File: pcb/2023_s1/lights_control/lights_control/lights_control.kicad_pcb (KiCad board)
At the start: 2 copper layers, 9 parts, among them J1 Conn_01x02_Male, Q1 TIP122, U1 4N25, U2 40106

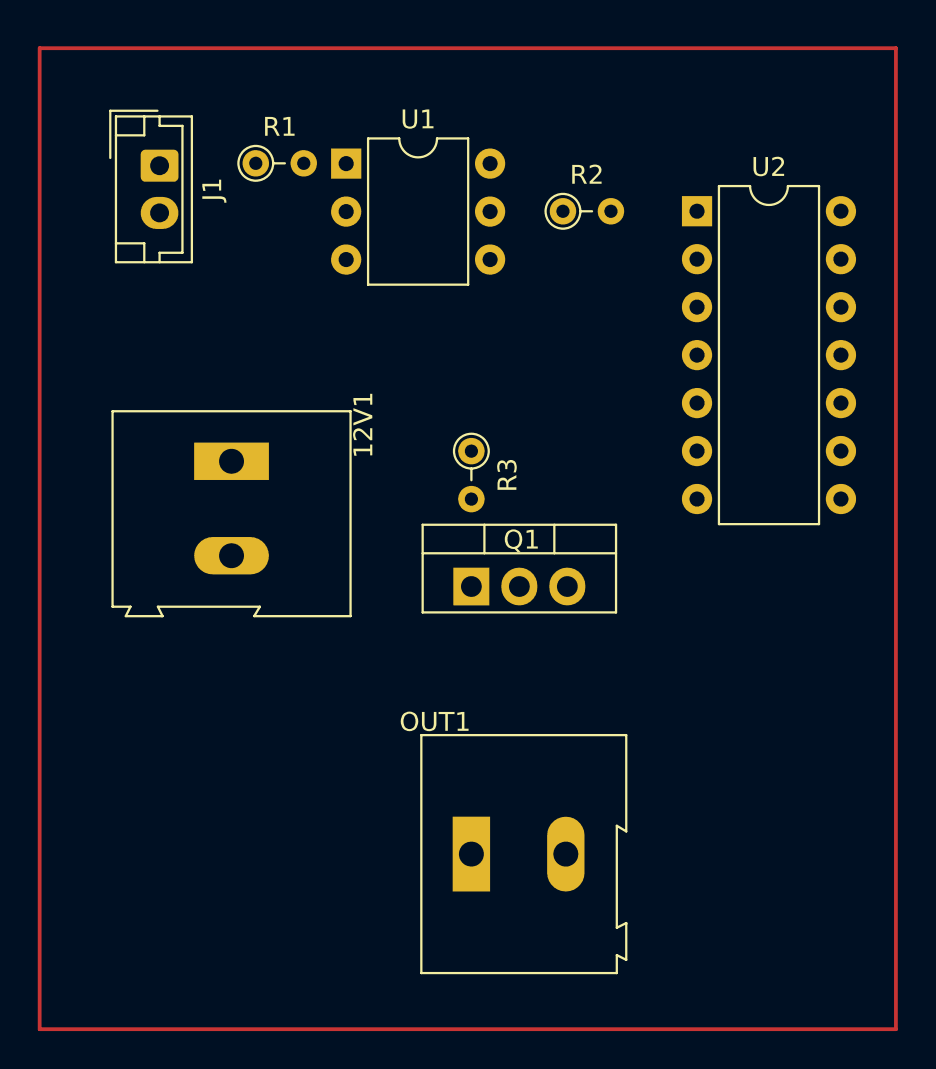
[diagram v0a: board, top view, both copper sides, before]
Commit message: addition, added 3 mounting holes to the pcb, need to add voltage reduction and a better transistor to turn on and off the led lights
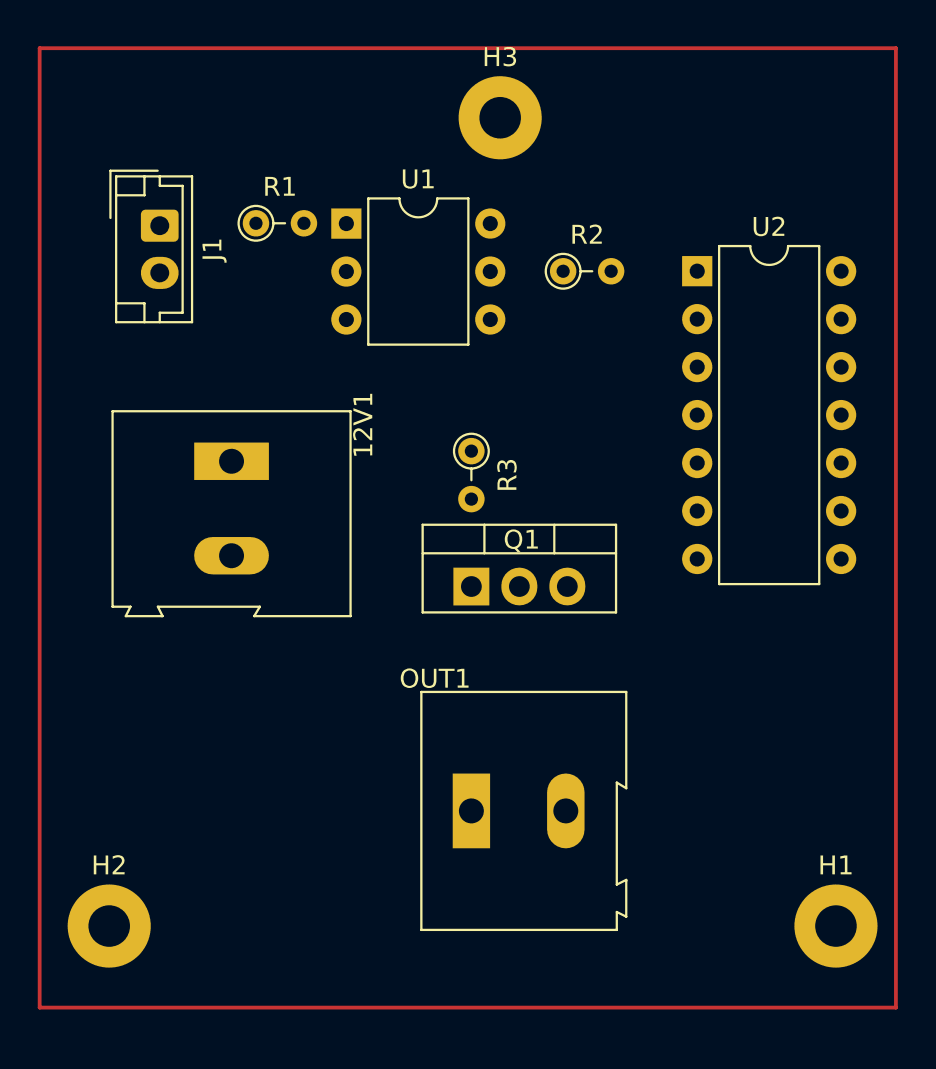
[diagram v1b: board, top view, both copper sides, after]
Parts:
- added H1: MountingHole, MountingHole:MountingHole_2.2mm_M2_Pad, F.Cu at (147.7, 116.1)
- added H2: MountingHole, MountingHole:MountingHole_2.2mm_M2_Pad, F.Cu at (109.2, 116.1)
- added H3: MountingHole, MountingHole:MountingHole_2.2mm_M2_Pad, F.Cu at (129.9, 73.3)
- moved R1 3.18 mm to (117.0, 78.9)
- moved U1 3.18 mm to (121.8, 78.9)
- moved J1 3.18 mm to (111.9, 79.0)
- moved R2 3.18 mm to (133.3, 81.4)
- moved U2 3.18 mm to (140.4, 81.4)
- moved OUT1 2.29 mm to (128.4, 110.0)
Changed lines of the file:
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@@
   (net 19 "unconnected-(U2-Pad10)")
   (net 20 "unconnected-(U2-Pad11)")
+  (footprint "MountingHole:MountingHole_2.2mm_M2_Pad" (layer "F.Cu")
+    (at 129.921 73.279)
+    (descr "Mounting Hole 2.2mm, M2")
+    (tags "mounting hole 2.2mm m2")
+    (property "Sheetfile" "lights_control.kicad_sch")
+    (property "Sheetname" "")
+    (attr exclude_from_pos_files)
+    (fp_text reference "H3" (at 0 -3.2) (layer "F.SilkS")
+      (effects (font (size 1 1) (thickness 0.15)))
+    )
+    (fp_text value "MountingHole" (at 0 3.2) (layer "F.Fab")
+      (effects (font (size 1 1) (thickness 0.15)))
+    )
+    (fp_text user "${REFERENCE}" (at 0 0) (layer "F.Fab")
+      (effects (font (size 1 1) (thickness 0.15)))
+    )
+    (fp_circle (center 0 0) (end 2.2 0) (layer "Cmts.User") (width 0.15) (fill none))
+    (fp_circle (center 0 0) (end 2.45 0) (layer "F.CrtYd") (width 0.05) (fill none))
+    (pad "1" thru_hole circle (at 0 0) (size 4.4 4.4) (drill 2.2) (layers *.Cu *.Mask))
+  )
   (footprint "TerminalBlock:TerminalBlock_Altech_AK300-2_P5.00mm" (layer "F.Cu")
     (at 115.697 91.469 -90)
@@
   )
   (footprint "Connector_JST:JST_EH_B2B-EH-A_1x02_P2.50mm_Vertical" (layer "F.Cu")
-    (at 111.887 75.819 -90)
+    (at 111.897 78.994 -90)
     (descr "JST EH series connector, B2B-EH-A (http://www.jst-mfg.com/product/pdf/eng/eEH.pdf), generated with kicad-footprint-generator")
     (tags "connector JST EH vertical")
@@
   )
   (footprint "Resistor_THT:R_Axial_DIN0204_L3.6mm_D1.6mm_P2.54mm_Vertical" (layer "F.Cu")
-    (at 116.981 75.692)
+    (at 116.991 78.867)
     (descr "Resistor, Axial_DIN0204 series, Axial, Vertical, pin pitch=2.54mm, 0.167W, length*diameter=3.6*1.6mm^2, http://cdn-reichelt.de/documents/datenblatt/B400/1_4W%23YAG.pdf")
     (tags "Resistor Axial_DIN0204 series Axial Vertical pin pitch 2.54mm 0.167W length 3.6mm diameter 1.6mm")
@@
   )
   (footprint "Package_DIP:DIP-14_W7.62mm" (layer "F.Cu")
-    (at 140.345 78.227)
+    (at 140.355 81.402)
     (descr "14-lead though-hole mounted DIP package, row spacing 7.62 mm (300 mils)")
     (tags "THT DIP DIL PDIP 2.54mm 7.62mm 300mil")
@@
     )
   )
+  (footprint "MountingHole:MountingHole_2.2mm_M2_Pad" (layer "F.Cu")
+    (at 147.701 116.078)
+    (descr "Mounting Hole 2.2mm, M2")
+    (tags "mounting hole 2.2mm m2")
+    (property "Sheetfile" "lights_control.kicad_sch")
+    (property "Sheetname" "")
+    (attr exclude_from_pos_files)
+    (fp_text reference "H1" (at 0 -3.2) (layer "F.SilkS")
+      (effects (font (size 1 1) (thickness 0.15)))
+    )
+    (fp_text value "MountingHole" (at 0 3.2) (layer "F.Fab")
+      (effects (font (size 1 1) (thickness 0.15)))
+    )
+    (fp_text user "${REFERENCE}" (at 0 0) (layer "F.Fab")
+      (effects (font (size 1 1) (thickness 0.15)))
+    )
+    (fp_circle (center 0 0) (end 2.2 0) (layer "Cmts.User") (width 0.15) (fill none))
+    (fp_circle (center 0 0) (end 2.45 0) (layer "F.CrtYd") (width 0.05) (fill none))
+    (pad "1" thru_hole circle (at 0 0) (size 4.4 4.4) (drill 2.2) (layers *.Cu *.Mask))
+  )
+  (footprint "MountingHole:MountingHole_2.2mm_M2_Pad" (layer "F.Cu")
+    (at 109.22 116.078)
+    (descr "Mounting Hole 2.2mm, M2")
+    (tags "mounting hole 2.2mm m2")
+    (property "Sheetfile" "lights_control.kicad_sch")
+    (property "Sheetname" "")
+    (attr exclude_from_pos_files)
+    (fp_text reference "H2" (at 0 -3.2) (layer "F.SilkS")
+      (effects (font (size 1 1) (thickness 0.15)))
+    )
+    (fp_text value "MountingHole" (at 0 3.2) (layer "F.Fab")
+      (effects (font (size 1 1) (thickness 0.15)))
+    )
+    (fp_text user "${REFERENCE}" (at 0 0) (layer "F.Fab")
+      (effects (font (size 1 1) (thickness 0.15)))
+    )
+    (fp_circle (center 0 0) (end 2.2 0) (layer "Cmts.User") (width 0.15) (fill none))
+    (fp_circle (center 0 0) (end 2.45 0) (layer "F.CrtYd") (width 0.05) (fill none))
+    (pad "1" thru_hole circle (at 0 0) (size 4.4 4.4) (drill 2.2) (layers *.Cu *.Mask))
+  )
   (footprint "Resistor_THT:R_Axial_DIN0204_L3.6mm_D1.6mm_P2.54mm_Vertical" (layer "F.Cu")
     (at 128.397 90.932 -90)
@@
   )
   (footprint "Package_DIP:DIP-6_W7.62mm" (layer "F.Cu")
-    (at 121.767 75.707)
+    (at 121.777 78.882)
     (descr "6-lead though-hole mounted DIP package, row spacing 7.62 mm (300 mils)")
     (tags "THT DIP DIL PDIP 2.54mm 7.62mm 300mil")
@@
   )
   (footprint "TerminalBlock:TerminalBlock_Altech_AK300-2_P5.00mm" (layer "F.Cu")
-    (at 128.397 112.268)
+    (at 128.397 109.982)
     (descr "Altech AK300 terminal block, pitch 5.0mm, 45 degree angled, see http://www.mouser.com/ds/2/16/PCBMETRC-24178.pdf")
     (tags "Altech AK300 terminal block pitch 5.0mm")
@@
   )
   (footprint "Resistor_THT:R_Axial_DIN0204_L3.6mm_D1.6mm_P2.54mm_Vertical" (layer "F.Cu")
-    (at 133.246 78.232)
+    (at 133.256 81.407)
     (descr "Resistor, Axial_DIN0204 series, Axial, Vertical, pin pitch=2.54mm, 0.167W, length*diameter=3.6*1.6mm^2, http://cdn-reichelt.de/documents/datenblatt/B400/1_4W%23YAG.pdf")
     (tags "Resistor Axial_DIN0204 series Axial Vertical pin pitch 2.54mm 0.167W length 3.6mm diameter 1.6mm")
@@
     )
   )
-  (gr_rect (start 150.876 69.596) (end 105.537 121.539) (layer "F.Cu") (width 0.2) (fill none))
+  (gr_rect (start 150.876 69.596) (end 105.537 120.396) (layer "F.Cu") (width 0.2) (fill none))
 )

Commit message: update, new export files and added voltage elevator space for lights control pcb
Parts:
- added H4: MountingHole, MountingHole:MountingHole_2.2mm_M2_Pad, F.Cu at (91.3, 116.2)
- added H5: MountingHole, MountingHole:MountingHole_2.2mm_M2_Pad, F.Cu at (64.0, 116.2)
- added H6: MountingHole, MountingHole:MountingHole_2.2mm_M2_Pad, F.Cu at (91.5, 59.1)
- added H7: MountingHole, MountingHole:MountingHole_2.2mm_M2_Pad, F.Cu at (64.2, 59.1)
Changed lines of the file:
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@@
     )
+  )
+  (footprint "MountingHole:MountingHole_2.2mm_M2_Pad" (layer "F.Cu")
+    (at 64.22 59.1)
+    (descr "Mounting Hole 2.2mm, M2")
+    (tags "mounting hole 2.2mm m2")
+    (property "Sheetfile" "lights_control.kicad_sch")
+    (property "Sheetname" "")
+    (attr exclude_from_pos_files)
+    (fp_text reference "H7" (at 0 -3.2) (layer "F.SilkS")
+      (effects (font (size 1 1) (thickness 0.15)))
+    )
+    (fp_text value "MountingHole" (at 0 3.2) (layer "F.Fab")
+      (effects (font (size 1 1) (thickness 0.15)))
+    )
+    (fp_text user "${REFERENCE}" (at 0 0) (layer "F.Fab")
+      (effects (font (size 1 1) (thickness 0.15)))
+    )
+    (fp_circle (center 0 0) (end 2.2 0) (layer "Cmts.User") (width 0.15) (fill none))
+    (fp_circle (center 0 0) (end 2.45 0) (layer "F.CrtYd") (width 0.05) (fill none))
+    (pad "1" thru_hole circle (at 0 0) (size 4.4 4.4) (drill 2.2) (layers *.Cu *.Mask))
   )
   (footprint "Package_TO_SOT_THT:TO-220-3_Vertical" (layer "F.Cu")
@@
       (rotate (xyz 0 0 0))
     )
+  )
+  (footprint "MountingHole:MountingHole_2.2mm_M2_Pad" (layer "F.Cu")
+    (at 64.02 116.2)
+    (descr "Mounting Hole 2.2mm, M2")
+    (tags "mounting hole 2.2mm m2")
+    (property "Sheetfile" "lights_control.kicad_sch")
+    (property "Sheetname" "")
+    (attr exclude_from_pos_files)
+    (fp_text reference "H5" (at 0 -3.2) (layer "F.SilkS")
+      (effects (font (size 1 1) (thickness 0.15)))
+    )
+    (fp_text value "MountingHole" (at 0 3.2) (layer "F.Fab")
+      (effects (font (size 1 1) (thickness 0.15)))
+    )
+    (fp_text user "${REFERENCE}" (at 0 0) (layer "F.Fab")
+      (effects (font (size 1 1) (thickness 0.15)))
+    )
+    (fp_circle (center 0 0) (end 2.2 0) (layer "Cmts.User") (width 0.15) (fill none))
+    (fp_circle (center 0 0) (end 2.45 0) (layer "F.CrtYd") (width 0.05) (fill none))
+    (pad "1" thru_hole circle (at 0 0) (size 4.4 4.4) (drill 2.2) (layers *.Cu *.Mask))
   )
   (footprint "Resistor_THT:R_Axial_DIN0204_L3.6mm_D1.6mm_P2.54mm_Vertical" (layer "F.Cu")
@@
       (rotate (xyz 0 0 0))
     )
+  )
+  (footprint "MountingHole:MountingHole_2.2mm_M2_Pad" (layer "F.Cu")
+    (at 91.3 116.2)
+    (descr "Mounting Hole 2.2mm, M2")
+    (tags "mounting hole 2.2mm m2")
+    (property "Sheetfile" "lights_control.kicad_sch")
+    (property "Sheetname" "")
+    (attr exclude_from_pos_files)
+    (fp_text reference "H4" (at 0 -3.2) (layer "F.SilkS")
+      (effects (font (size 1 1) (thickness 0.15)))
+    )
+    (fp_text value "MountingHole" (at 0 3.2) (layer "F.Fab")
+      (effects (font (size 1 1) (thickness 0.15)))
+    )
+    (fp_text user "${REFERENCE}" (at 0 0) (layer "F.Fab")
+      (effects (font (size 1 1) (thickness 0.15)))
+    )
+    (fp_circle (center 0 0) (end 2.2 0) (layer "Cmts.User") (width 0.15) (fill none))
+    (fp_circle (center 0 0) (end 2.45 0) (layer "F.CrtYd") (width 0.05) (fill none))
+    (pad "1" thru_hole circle (at 0 0) (size 4.4 4.4) (drill 2.2) (layers *.Cu *.Mask))
   )
   (footprint "Package_DIP:DIP-6_W7.62mm" (layer "F.Cu")
@@
     )
   )
-  (gr_rect (start 150.876 69.596) (end 105.537 120.396) (layer "F.Cu") (width 0.2) (fill none))
+  (footprint "MountingHole:MountingHole_2.2mm_M2_Pad" (layer "F.Cu")
+    (at 91.5 59.1)
+    (descr "Mounting Hole 2.2mm, M2")
+    (tags "mounting hole 2.2mm m2")
+    (property "Sheetfile" "lights_control.kicad_sch")
+    (property "Sheetname" "")
+    (attr exclude_from_pos_files)
+    (fp_text reference "H6" (at 0 -3.2) (layer "F.SilkS")
+      (effects (font (size 1 1) (thickness 0.15)))
+    )
+    (fp_text value "MountingHole" (at 0 3.2) (layer "F.Fab")
+      (effects (font (size 1 1) (thickness 0.15)))
+    )
+    (fp_text user "${REFERENCE}" (at 0 0) (layer "F.Fab")
+      (effects (font (size 1 1) (thickness 0.15)))
+    )
+    (fp_circle (center 0 0) (end 2.2 0) (layer "Cmts.User") (width 0.15) (fill none))
+    (fp_circle (center 0 0) (end 2.45 0) (layer "F.CrtYd") (width 0.05) (fill none))
+    (pad "1" thru_hole circle (at 0 0) (size 4.4 4.4) (drill 2.2) (layers *.Cu *.Mask))
+  )
+  (gr_rect (start 150.876 52.346) (end 56.287 121.396) (layer "F.Cu") (width 0.2) (fill none))
+  (gr_rect (start 59.4 54.85) (end 96.25 120) (layer "F.SilkS") (width 0.2) (fill none))
+  (group "" (id 00337593-777a-4c58-88cc-cdb5a021b062)
+    (members
+      187c98bf-b8d1-4bf8-a18b-adc7ccf804a8
+      e91737d2-66c0-4c66-9fda-42e3aaefe411
+    )
+  )
+  (group "" (id 7de41c36-1b53-434b-914d-120d0a8890b0)
+    (members
+      6e19ae29-2da6-47ad-aa21-1ab7fbc4f013
+      985ad4b4-784b-4b28-a9a1-c418e2ce8c57
+    )
+  )
 )

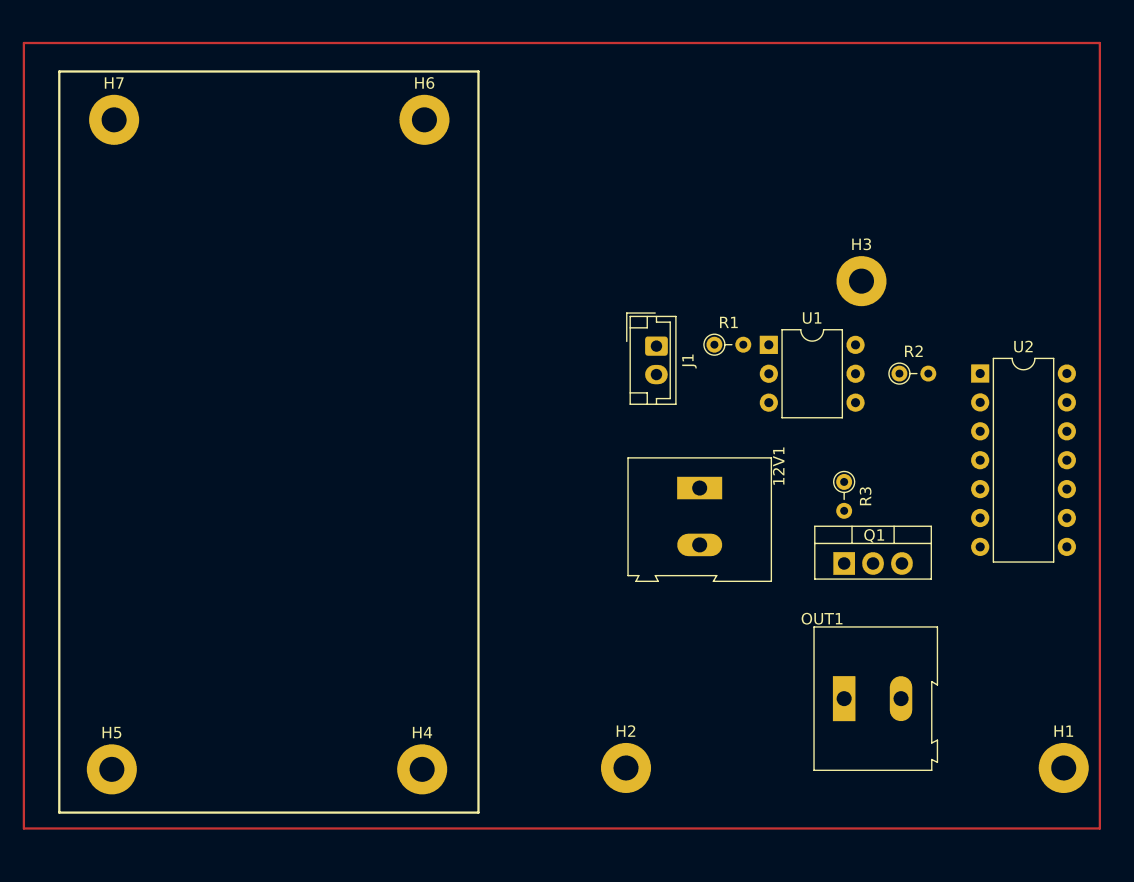
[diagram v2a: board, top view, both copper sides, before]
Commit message: update, routed lights pcb
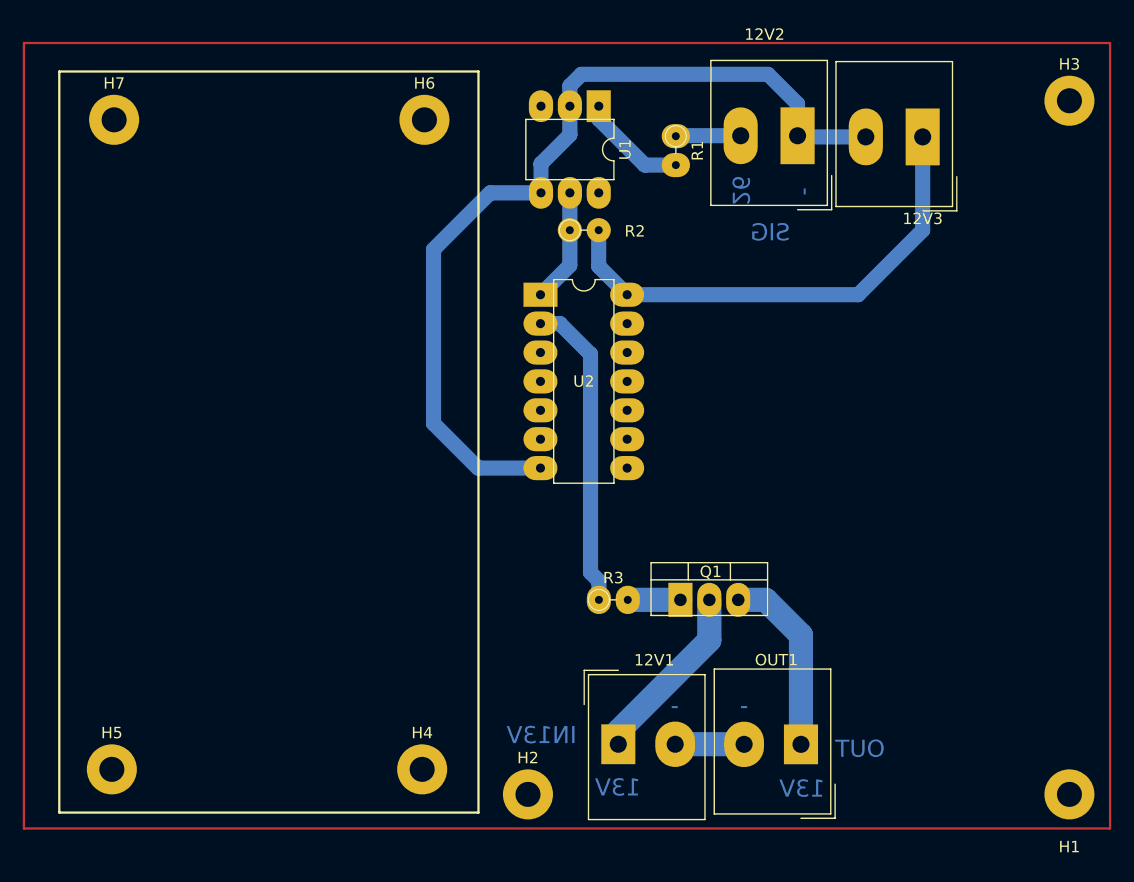
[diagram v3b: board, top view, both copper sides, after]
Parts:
- removed J1: Conn_01x02_Male, Connector_JST:JST_EH_B2B-EH-A_1x02_P2.50mm_Vertical
- added 12V2: Screw_Terminal_01x02, TerminalBlock_Altech:Altech_AK300_1x02_P5.00mm_45-Degree, F.Cu at (124.3, 60.5)
- added 12V3: Screw_Terminal_01x02, TerminalBlock_Altech:Altech_AK300_1x02_P5.00mm_45-Degree, F.Cu at (135.3, 60.6)
- 12V1, OUT1: footprint TerminalBlock:TerminalBlock_Altech_AK300-2_P5.00mm -> TerminalBlock_Altech:Altech_AK300_1x02_P5.00mm_45-Degree
- moved U2 39.3 mm to (101.7, 74.5)
- moved R2 31.6 mm to (104.3, 68.8)
- moved U1 25.8 mm to (106.8, 57.9), turned to -90 degrees
- moved H3 24.2 mm to (148.2, 57.4)
- moved R3 23.9 mm to (106.8, 101.3), turned to 0 degrees
- moved 12V1 23.6 mm to (108.5, 114.0), turned to 0 degrees
- moved R1 18.6 mm to (113.6, 60.5), turned to -90 degrees
- moved Q1 14.7 mm to (114.0, 101.3)
- moved H2 8.93 mm to (100.6, 118.4)
- moved OUT1 5.53 mm to (124.6, 114.0), turned to 180 degrees
- moved H1 2.38 mm to (148.2, 118.4)
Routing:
- net GND5V: track 0.00 -> 78.6 mm
- net 5v: track 0.00 -> 43.2 mm
- net Net-(R3-Pad1): track 0.00 -> 27.4 mm
- net Net-(OUT1-Pad1): track 0.00 -> 16.4 mm
- net 12v: track 0.00 -> 16.0 mm
- net Net-(R2-Pad1): track 0.00 -> 10.0 mm
- net Net-(R1-Pad2): track 0.00 -> 9.58 mm
- net GND12V: track 0.00 -> 6.06 mm
- net D26: track 0.00 -> 5.72 mm
- net Net-(Q1-Pad1): track 0.00 -> 4.63 mm
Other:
- board text added: "-"
- board text added: "13V"
- board text added: "26"
- board text added: "IN13V"
- board text added: "OUT"
- board text added: "SIG"

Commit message: update, fixed lights pcb, only lacks rerouting
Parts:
- removed 12V3: Screw_Terminal_01x02, TerminalBlock_Altech:Altech_AK300_1x02_P5.00mm_45-Degree
- moved R1 2.72 mm to (112.8, 57.9)
- moved OUT1 0.41 mm to (124.7, 114.4)
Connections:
- 12V2 pad 1: GND5V -> GND SIG
- R2 pad 2: 5v -> 12v
- U1 pad 2: GND5V -> GND SIG
- U1 pad 4: GND5V -> GND12V
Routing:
- net GND5V: track 78.6 -> 0.00 mm
- net 5v: track 43.2 -> 0.00 mm
- net Net-(R3-Pad1): track 27.4 -> 0.00 mm
- net GND SIG: track 0.00 -> 27.3 mm
- net 12v: track 16.0 -> 39.0 mm
- net Net-(OUT1-Pad1): track 16.4 -> 0.00 mm
- net GND12V: track 6.06 -> 0.01 mm
- net Net-(Q1-Pad1): track 4.63 -> 0.00 mm
- net Net-(R1-Pad2): track 9.58 -> 7.04 mm
- net D26: track 5.72 -> 7.56 mm
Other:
- board text added: "Building an open agricultue. Today."
- board text added: "Maticas Light control module"
- board text added: "Voltage Elevator"

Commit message: fix, the trigger schmith was not powered in the PCB
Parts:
- moved H3 17.1 mm to (131.2, 55.8)
- moved H1 17.0 mm to (131.2, 118.0)
- moved H2 0.40 mm to (100.6, 118.0)
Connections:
- U2 pad 14: 5v -> 12v
- U2 pad 7: GND5V -> GND12V
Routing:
- net GND12V: track 0.01 -> 91.3 mm
- net Net-(R3-Pad1): track 0.00 -> 27.9 mm
- net 12v: track 39.0 -> 60.8 mm
- net Net-(OUT1-Pad1): track 0.00 -> 15.4 mm
- net Net-(Q1-Pad1): track 0.00 -> 4.63 mm
